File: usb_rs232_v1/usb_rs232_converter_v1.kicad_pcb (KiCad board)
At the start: 2 copper layers, 59 x 40 mm, 46 parts, among them CON1 USB-micro-B, IC1 MAX3243, IC2 FT232BL, J1 COM LEFT, J2 COM RIGHT, J3 FTDI, J4 UART

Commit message: PCB v1.0 BIG
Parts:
- removed COM1: COM LEFT COM, SIL-8-SMD
- removed COM2: COM RIGHT COM, SIL-8
- removed COM3: COM RIGHT FTDI, SIL-8-SMD
- added CON2: USB-mini-B, usb-mini-B-2, B.Cu at (160.0, 118.5)
- added F1: FUSE, SM1812, B.Cu at (149.4, 109.8)
- added J5: UART, SIL-4, F.Cu at (161.4, 103.4)
- added J6: COM LEFT COM, SIL-8, F.Cu at (130.8, 97.5)
- added J7: COM RIGHT COM, SIL-8, F.Cu at (192.5, 97.5)
- added R10: 0R, SM0603, B.Cu at (141.6, 113.4)
- added R11: 0R, SM0603, B.Cu at (164.3, 100.4)
- added R8: 0R, SM0805, B.Cu at (149.4, 115.4)
- added R9: 0R, SM1206, B.Cu at (156.4, 111.0)
- C11, C7: moved to B.Cu
- C2, C3: moved to F.Cu
- C4: footprint SM0603_Capa -> SM1206
- J4: value UART -> COM RIGHT FTDI; footprint SIL-4-SMD -> SIL-8
- moved C10 101.8 mm to (170.8, 88.2), turned to 270 degrees
- moved C8 101.4 mm to (164.1, 86.0), turned to 0 degrees
- moved C5 101.1 mm to (162.6, 91.6), turned to 0 degrees
- moved C7 99.5 mm to (167.6, 86.0), turned to 0 degrees
- moved C4 97.7 mm to (162.6, 94.2), turned to 0 degrees
- moved C11 96.4 mm to (160.1, 88.7), turned to 270 degrees
- moved C3 96.0 mm to (150.0, 97.2), turned to 0 degrees
- moved C12 94.6 mm to (149.0, 89.6), turned to 270 degrees
- moved R4 89.6 mm to (143.9, 95.8)
- moved C2 87.6 mm to (150.0, 99.6), turned to 180 degrees
- moved R3 82.5 mm to (141.6, 109.2), turned to 90 degrees
- moved R1 82.3 mm to (148.2, 102.8), turned to 0 degrees
- moved L1 82.2 mm to (144.6, 106.8)
- moved C9 80.2 mm to (153.0, 103.2), turned to 180 degrees
- moved R2 78.7 mm to (139.4, 109.2), turned to 90 degrees
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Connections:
- C3 pad 1: /USB Vcc -> VCC
- CON1 pad 1: GND -> N-000008
- CON1 pad 2: (no net) -> /D-
- CON1 pad 4: /D- -> (no net)
- CON1 pad 5: /USB Vcc -> N-0000052
- J3 pad 1: /Tout: TxD -> /Rin: RI
- J3 pad 2: /Rin: RxD -> /Rin: DCD
- J3 pad 3: /Tout: RST -> /Rin: DSR
- J3 pad 5: /Tout: DTR -> /Rin: RxD
- J3 pad 6: /Rin: DSR -> /Tout: TxD
- J3 pad 7: /Rin: DCD -> /Tout: DTR
- J3 pad 8: /Rin: RI -> /Tout: RST
- J4 pad 1: VCC -> /RI COM
- J4 pad 2: /Tin: TxD -> /DCD COM
- J4 pad 3: /Rout: RxD -> /DSR COM
- J4 pad 4: GND -> /CTS COM
- L1 pad 1: /USB Vcc -> N-0000054
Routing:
- net GND: track 0.00 -> 200.2 mm, vias 0 -> 6
- net VCC: track 0.00 -> 97.3 mm, vias 0 -> 2
- net /RST COM: track 29.4 -> 115.4 mm
- net /RxD COM: track 16.8 -> 97.1 mm
- net /TxD COM: track 16.3 -> 95.0 mm, vias 1 -> 0
- net /CTS COM: track 31.3 -> 104.9 mm
- net /DTR COM: track 31.3 -> 99.7 mm
- net /DSR COM: track 48.9 -> 100.6 mm
- net /RI COM: track 53.2 -> 99.4 mm
- net /D-: track 0.00 -> 38.0 mm
- net /D+: track 0.00 -> 30.8 mm
- net /D--: track 0.00 -> 23.4 mm
- net /DCD COM LEFT: track 0.00 -> 23.3 mm
- net /RX LED: track 0.00 -> 23.2 mm, vias 0 -> 1
- net /Rin: RI: track 0.00 -> 22.0 mm
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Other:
- board size 59 x 40 mm -> 85 x 51 mm

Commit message: PCB v1.1 poligony
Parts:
- added SIL-1: Val**, SIL-1, F.Cu at (37.5, 31.0)
- added SIL-1: Val**, SIL-1, F.Cu at (36.0, 59.0)
- added SIL-1: Val**, SIL-1, F.Cu at (51.0, 22.0)
- added SIL-1: Val**, SIL-1, F.Cu at (25.0, 41.0)
- added SIL-1: Val**, SIL-1, F.Cu at (96.5, 63.0)
- added SIL-1: Val**, SIL-1, F.Cu at (94.5, 25.5)
- moved C10 109.9 mm to (74.3, 35.7)
- moved D2 109.9 mm to (67.3, 45.9)
- moved R11 109.9 mm to (67.8, 47.9)
- moved R7 109.9 mm to (65.3, 45.9)
- moved C11 109.9 mm to (63.6, 36.2)
- moved C12 109.9 mm to (52.5, 37.1)
- moved C2 109.9 mm to (53.5, 47.1)
- moved C3 109.9 mm to (53.5, 44.7)
- moved C4 109.9 mm to (66.1, 41.7)
- moved C5 109.9 mm to (66.1, 39.1)
- moved C7 109.9 mm to (71.1, 33.5)
- moved C8 109.9 mm to (67.6, 33.5)
- moved C9 109.9 mm to (56.5, 50.7)
- moved CON1 109.9 mm to (45.2, 69.5)
- moved CON2 109.9 mm to (63.5, 66.0)
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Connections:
- CON1 pad 8: (no net) -> GND
- CON2 pad 9: (no net) -> GND
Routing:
- net GND: track 200.2 -> 234.6 mm, vias 6 -> 7
- net VCC: track 97.3 -> 99.9 mm
- net /RST COM LEFT: track 14.2 -> 13.3 mm
- net /DCD COM LEFT: track 23.3 -> 24.1 mm
- added copper zone on B.Cu, net GND
- added copper zone on F.Cu, net GND

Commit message: usb_rs232 pcb_v2.0
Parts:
- removed D11: RED, LED-3MM-SMD
- removed D12: GREEN, LED-3MM-SMD
- removed D13, D14, D15, D16, D17, D18: YELLOW, LED-3MM-SMD
- removed J5: UART, SIL-4
- removed R1, R20, R21, R22: 470R, SM0805
- removed R2, R3: 27R, SM0805
- removed R4: 1k5, SM1206
- removed R9: 0R, SM1206
- removed SIL-1 (x6): Val**, SIL-1
- added C1: 27p, SM0603, B.Cu at (183.8, 64.8)
- added C13: 100n, SM0603, B.Cu at (177.5, 42.0)
- added C14: 100n, SM0603, B.Cu at (175.8, 46.8)
- added C15: 4n7, SM1206, F.Cu at (168.5, 73.8)
- added C16: 100n, SM0603, F.Cu at (172.0, 42.0)
- added C6: 100n, SM0603, F.Cu at (172.0, 58.0)
- added D10: RI, LED-3MM-SMD, F.Cu at (198.0, 37.0)
- added D3: TxD, LED-3MM-SMD, F.Cu at (198.0, 62.0)
- added D4: RxD, LED-3MM-SMD, F.Cu at (198.0, 57.0)
- added D5: RTS, LED-3MM-SMD, F.Cu at (198.0, 72.0)
- added D6: CTS, LED-3MM-SMD, F.Cu at (198.0, 52.0)
- added D7: DTR, LED-3MM-SMD, F.Cu at (198.0, 67.0)
- added D8: DSR, LED-3MM-SMD, F.Cu at (198.0, 47.0)
- added D9: DCD, LED-3MM-SMD, F.Cu at (198.0, 42.0)
- added F2: 500mA, SM1206, F.Cu at (165.0, 73.8)
- added J8: COM RIGHT FTDI, SIL-8_bigger_hole, F.Cu at (209.5, 54.5)
- added R12: 470R, SM0805, F.Cu at (191.0, 57.0)
- added R13: 470R, SM0805, F.Cu at (191.0, 54.0)
- added R14: 470R, SM0805, F.Cu at (191.0, 63.0)
- added VR1: MC78L33, sot89, B.Cu at (171.8, 47.5)
- added X1: QUARTZCMS4_M, Q_49U3HMS, B.Cu at (185.8, 68.2)
- C10, C7, C8: value C -> 100n; footprint SM0603_Capa -> SM0603
- C11: value C -> 100n; footprint SM0603_Capa -> SM0603; moved to F.Cu
- C12: value 33n -> 100n; footprint SM0805 -> SM0603; moved to F.Cu
- C2: value 100n -> 33n; footprint SM0603_Capa -> SM0805; moved to B.Cu
- C3: value 10u -> 27p; footprint SM1206POL -> SM0603; moved to B.Cu
- C4: value 100n -> 10u; footprint SM1206 -> SM1206POL
- C5: value 10u -> 100n; footprint SM1206POL -> SM0603; moved to B.Cu
- C9: footprint SM0603_Capa -> SM0603; moved to F.Cu
- F1: value FUSE -> 500mA; footprint SM1812 -> SM1206; moved to F.Cu
- IC1: value MAX3243 -> FT232BL; footprint tssop-28 -> TQFP32
- IC2: value FT232BL -> MAX3243; footprint TQFP32 -> tssop-28
- J2: value COM RIGHT -> COM LEFT COM; footprint DB9MC-v2 -> SIL-8_bigger_hole; moved to F.Cu
- J3: value FTDI -> COM RIGHT COM; footprint SIL-8 -> SIL-8_bigger_hole
- J4: value COM RIGHT FTDI -> UART; footprint SIL-8 -> SIL-5_bigger_holes
- J6: value COM LEFT COM -> COM RIGHT; footprint SIL-8 -> DB9MC-v2; moved to B.Cu
- J7: value COM RIGHT COM -> FTDI; footprint SIL-8 -> SIL-8_bigger_hole
- L1: value INDUCTOR_SMALL -> 15uH; moved to F.Cu
- R10, R11: value 0R -> 470R; footprint SM0603 -> SM0805
- R5, R6: value R -> 27R; moved to B.Cu
- R7: value 0R -> 1k5; footprint SM0603 -> SM1210
- R8: value 0R -> 470R; footprint SM0805 -> SM1206; moved to F.Cu
- moved J6 180.5 mm to (214.5, 54.5), turned to 90 degrees
- moved J4 140.6 mm to (177.2, 39.5), turned to 180 degrees
- moved C3 136.0 mm to (188.0, 64.8), turned to 180 degrees
- moved R10 134.4 mm to (178.8, 46.8), turned to 90 degrees
- moved C12 132.7 mm to (184.1, 54.4)
- moved CON1 131.1 mm to (176.0, 79.0)
- moved C9 129.4 mm to (185.8, 54.4), turned to 90 degrees
- moved IC2 128.7 mm to (185.1, 57.1), turned to 270 degrees
- moved L1 127.1 mm to (174.8, 64.8)
- moved C8 124.1 mm to (190.2, 53.1), turned to 90 degrees
- moved F1 122.5 mm to (174.8, 70.2)
- moved C11 120.1 mm to (182.3, 54.4)
- moved R8 118.9 mm to (171.8, 64.8)
- moved R19 116.9 mm to (191.0, 42.0)
- moved R16 116.7 mm to (191.0, 60.0)
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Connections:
- C10 pad 1: GND -> +3.3V
- C10 pad 2: N-0000034 -> GND
- C11 pad 1: N-000006 (its old number) -> N-000001
- C11 pad 2: VCC -> N-000005
- C12 pad 1: GND -> N-0000010
- C12 pad 2: N-000001 -> GND
- C2 pad 2: VCC -> N-0000034
- C3 pad 1: VCC -> /XTOUT
- C4 pad 1: VCC -> +5V
- C5 pad 1: VCC -> GND
- C5 pad 2: GND -> /AVCC
- C7 pad 1: N-000004 -> GND
- C7 pad 2: N-000005 -> +3.3V
- C8 pad 1: N-0000033 -> N-000008
- C8 pad 2: N-0000032 -> N-000009
- C9 pad 2: N-0000055 -> N-000007
- CON1 pad 1: N-000008 -> N-0000057
- CON1 pad 5: N-0000052 -> N-0000039
- CON1 pad 8: GND -> N-0000039
- CON2 pad 1: /USB Vcc -> N-0000057
- CON2 pad 6: (no net) -> N-0000039
- CON2 pad 9: GND -> (no net)
- D1 pad 1: N-0000026 -> N-0000012
- D2 pad 1: N-0000025 -> N-0000011
- F1 pad 1: /USB Vcc -> N-0000057
- IC1 pad 1: N-000005 -> (no net)
- IC1 pad 10: /Tout: DTR -> (no net)
- IC1 pad 11: /Tout: RST -> /RX LED
- IC1 pad 12: /Tin: RST2 -> /TX LED
- IC1 pad 13: /Tin: DTR -> +3.3V
- IC1 pad 14: /Tin: TxD -> GND
- IC1 pad 15: /Rout: RxD -> (no net)
- IC1 pad 16: /Rout: CTS -> (no net)
- IC1 pad 17: /Rout: DSR -> GND
- IC1 pad 18: /Rout: DCD -> /Rout: RI
- IC1 pad 19: /Rout: RI -> /Rout: DCD
- IC1 pad 2: N-000004 -> (no net)
- IC1 pad 20: (no net) -> /Rout: DSR
- IC1 pad 21: (no net) -> /Tin: DTR
- IC1 pad 22: VCC -> /Rout: CTS
- IC1 pad 23: VCC -> /Tin: RST
- IC1 pad 24: N-0000032 -> /Rout: RxD
- IC1 pad 25: GND -> /Tin: TxD
- IC1 pad 26: VCC -> +5V
- IC1 pad 27: N-000006 (its old number) -> /XTIN
- IC1 pad 28: N-0000033 -> /XTOUT
- IC1 pad 3: N-0000034 -> +5V
- IC1 pad 4: /Rin: RI -> (no net)
- IC1 pad 5: /Rin: DCD -> (no net)
- IC1 pad 6: /Rin: DSR -> N-0000034
- IC1 pad 7: /Rin: CTS -> /D++
- IC1 pad 8: /Rin: RxD -> /D--
- IC1 pad 9: /Tout: TxD -> GND
- IC2 pad 1: (no net) -> N-000009
- IC2 pad 10: (no net) -> /Tout: DTR
- IC2 pad 11: /RX LED -> /Tout: RST
- IC2 pad 12: /TX LED -> /Tin: RST
- IC2 pad 13: VCC -> /Tin: DTR
- IC2 pad 14: (no net) -> /Tin: TxD
- IC2 pad 15: (no net) -> /Rout: RxD
- IC2 pad 16: (no net) -> /Rout: CTS
- IC2 pad 17: GND -> /Rout: DSR
- IC2 pad 18: /Rout: RI -> /Rout: DCD
- IC2 pad 19: /Rout: DCD -> /Rout: RI
- IC2 pad 2: (no net) -> N-000008
- IC2 pad 20: /Rout: DSR -> (no net)
- IC2 pad 21: /Tin: DTR -> (no net)
- IC2 pad 22: /Rout: CTS -> +3.3V
- IC2 pad 23: /Tin: RST -> +3.3V
- IC2 pad 24: /Rout: RxD -> N-000005
- IC2 pad 25: /Tin: TxD -> GND
- IC2 pad 26: VCC -> +3.3V
- IC2 pad 27: (no net) -> N-0000010
- IC2 pad 28: (no net) -> N-000001
- IC2 pad 3: VCC -> N-000007
- IC2 pad 4: VCC -> /Rin: RI
- IC2 pad 5: N-000002 -> /Rin: DCD
- IC2 pad 6: N-000001 -> /Rin: DSR
- IC2 pad 7: /D++ -> /Rin: CTS
- IC2 pad 8: /D-- -> /Rin: RxD
- IC2 pad 9: GND -> /Tout: TxD
- J2 pad 1: /DCD COM -> /RI COM LEFT
- J2 pad 2: /RxD COM -> /DCD COM LEFT
- J2 pad 3: /TxD COM -> /DSR COM LEFT
- J2 pad 4: /DTR COM -> /CTS COM LEFT
- J2 pad 5: GND -> /RxD COM LEFT
- J2 pad 6: /DSR COM -> /TxD COM LEFT
- J2 pad 7: /RST COM -> /DTR COM LEFT
- J2 pad 8: /CTS COM -> /RST COM LEFT
- J3 pad 1: /Rin: RI -> /RI COM
- J3 pad 2: /Rin: DCD -> /DCD COM
- J3 pad 3: /Rin: DSR -> /DSR COM
- J3 pad 4: /Rin: CTS -> /CTS COM
- J3 pad 5: /Rin: RxD -> /RxD COM
- J3 pad 6: /Tout: TxD -> /TxD COM
- J3 pad 7: /Tout: DTR -> /DTR COM
- J3 pad 8: /Tout: RST -> /RST COM
- J4 pad 1: /RI COM -> +5V
- J4 pad 2: /DCD COM -> +3.3V
- J4 pad 3: /DSR COM -> /Rout: RxD
- J4 pad 4: /CTS COM -> /Tin: TxD
- J4 pad 5: /RxD COM -> GND
- J6 pad 1: /RI COM LEFT -> /DCD COM
- J6 pad 2: /DCD COM LEFT -> /RxD COM
- J6 pad 3: /DSR COM LEFT -> /TxD COM
- J6 pad 4: /CTS COM LEFT -> /DTR COM
- J6 pad 5: /RxD COM LEFT -> GND
- J6 pad 6: /TxD COM LEFT -> /DSR COM
- J6 pad 7: /DTR COM LEFT -> /RST COM
- J6 pad 8: /RST COM LEFT -> /CTS COM
- J7 pad 1: /RI COM -> /Rin: RI
- J7 pad 2: /DCD COM -> /Rin: DCD
- J7 pad 3: /DSR COM -> /Rin: DSR
- J7 pad 4: /CTS COM -> /Rin: CTS
- J7 pad 5: /RxD COM -> /Rin: RxD
- J7 pad 6: /TxD COM -> /Tout: TxD
- J7 pad 7: /DTR COM -> /Tout: DTR
- J7 pad 8: /RST COM -> /Tout: RST
- L1 pad 2: VCC -> +5V
- R10 pad 1: GND -> +3.3V
- R10 pad 2: N-0000052 -> N-0000012
- R11 pad 1: /Rout: RxD -> +3.3V
- R11 pad 2: N-0000053 -> N-0000011
- R5 pad 1: VCC -> /D-
- R5 pad 2: N-0000026 -> /D--
- R6 pad 1: VCC -> /D+
- R6 pad 2: N-0000025 -> /D++
- R7 pad 1: /Tin: RST2 -> N-0000034
- R7 pad 2: /Tin: RST -> /D++
- R8 pad 1: /USB Vcc -> +5V
- R8 pad 2: N-000008 -> /AVCC
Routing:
- net GND: track 234.6 -> 336.6 mm, vias 7 -> 11
- net VCC: track 99.9 -> 0.00 mm, vias 2 -> 0
- net +5V: track 0.00 -> 66.1 mm, vias 0 -> 2
- net +3.3V: track 0.00 -> 50.2 mm
- net /Tin: TxD: track 21.3 -> 62.7 mm
- net /Rout: RxD: track 10.2 -> 39.6 mm
- net N-0000057: track 0.00 -> 28.8 mm, vias 0 -> 1
- net /XTOUT: track 0.00 -> 27.9 mm
- net /DTR COM: track 99.7 -> 125.6 mm, vias 0 -> 2
- net N-0000039: track 4.43 -> 29.8 mm, vias 0 -> 2
- net /TxD COM: track 95.0 -> 114.0 mm
- net /USB Vcc: track 18.5 -> 0.00 mm
- net /XTIN: track 0.00 -> 17.8 mm
- net N-0000035: track 15.4 -> 0.00 mm
- net /DSR COM: track 100.6 -> 114.8 mm
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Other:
- outline, holes or cut-outs redrawn
- net class Default: trace_width 0.3556 -> 0.254; via_dia 1.3 -> 0.9; via_drill 0.9 -> 0.6
- net class power removed
- net class signal added: clearance 0.2032, trace_width 0.254, via_dia 0.9, via_drill 0.6
- net class small track removed
- net class supply added: clearance 0.2032, trace_width 0.7112, via_dia 1.2, via_drill 0.9
- rule via_min_drill: 0.9 -> 0.508
- rule via_min_size: 1.3 -> 0.889
- board text added: "3V3"
- board text added: "5V"
- board text added: "CTS"
- board text added: "DCD"
- board text added: "DSR"
- board text added: "DTR"
- board text added: "GDN"
- board text added: "RI"
- board text added: "RTS"
- board text added: "RxD"
- board text added: "TxD"
- board text added: "UART RxD"
- board text added: "UART TxD"

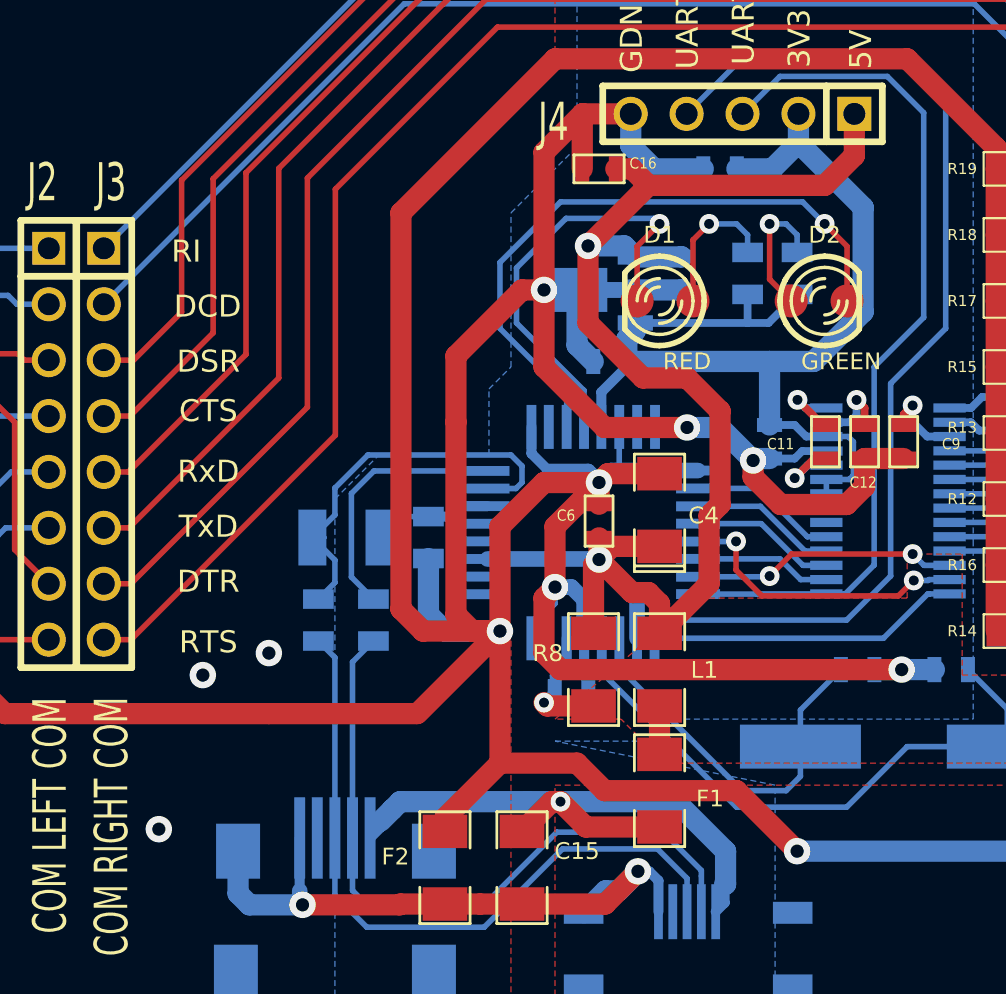
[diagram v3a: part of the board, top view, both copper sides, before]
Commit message: usb_rs232: v2.1: poprawiony footprint VR1
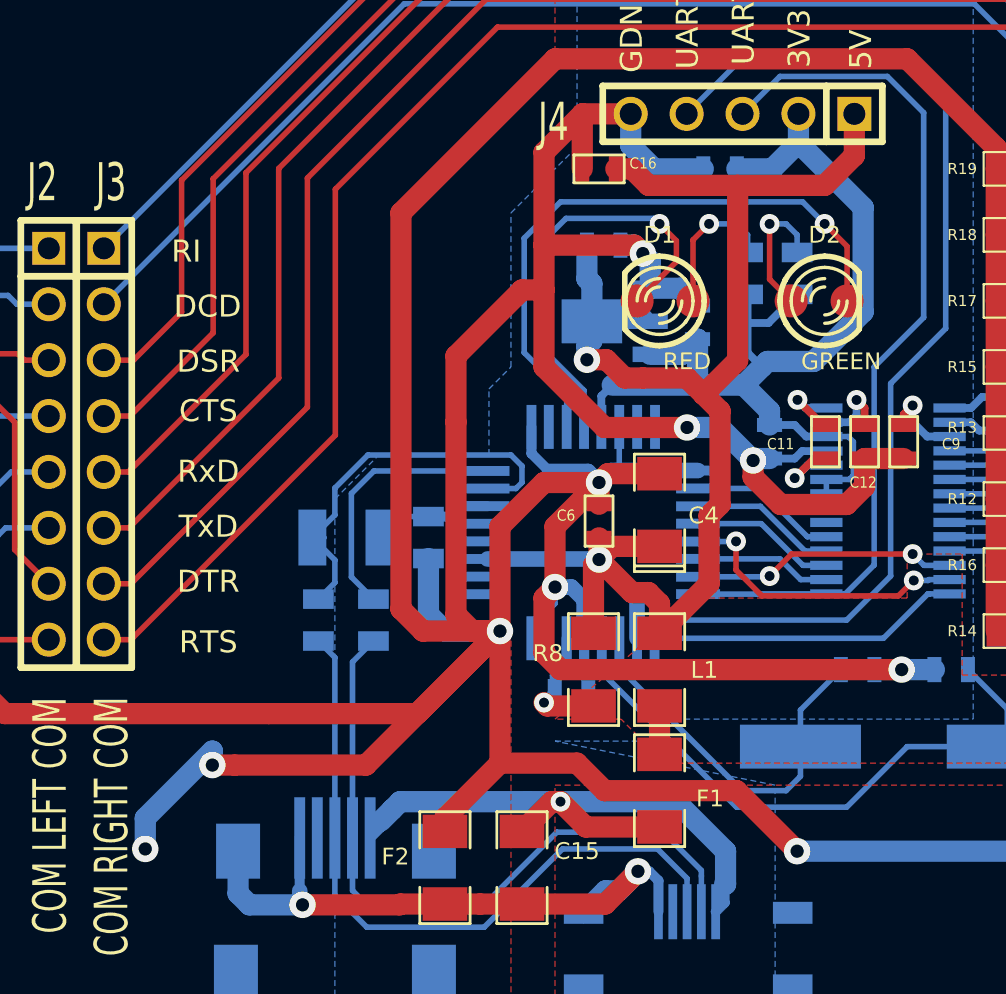
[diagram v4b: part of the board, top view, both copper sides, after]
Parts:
- moved C7 4.35 mm to (176.5, 49.0), turned to 270 degrees
- moved C14 3.76 mm to (172.2, 45.5), turned to 180 degrees
- moved VR1 1.58 mm to (172.4, 48.9)
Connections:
- VR1 pad 1: +5V -> GND
- VR1 pad 2: GND -> +5V
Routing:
- net GND: track 336.6 -> 359.2 mm, vias 11 -> 10
- net +5V: track 66.1 -> 71.6 mm
- net /RX LED: track 29.0 -> 28.0 mm
- net +3.3V: track 50.2 -> 49.4 mm
